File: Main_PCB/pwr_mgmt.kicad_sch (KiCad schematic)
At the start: 22 parts, among them SW201 SW_SPST, U201 TPS2116DRL, U202 TPS62143, U203 AP2112K-3.3

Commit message: First draft of schematic complete. Still need to verify it is correct before proceeding to pcb.
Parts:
- removed BT201, BT202: Battery_Cell, symbol Device:Battery_Cell
- removed C202, C204: 10uF, symbol Device:C
- removed C207: 100nF, symbol Device:C
- removed D201: LED, symbol Device:LED
- removed F201: Fuse, symbol Device:Fuse
- removed R201: 100K, symbol Device:R
- removed R204: 220R, symbol Device:R
- removed SW201: SW_SPST, symbol Switch:SW_SPST
- removed U203: AP2112K-3.3, Package_TO_SOT_SMD:SOT-23-5, symbol Regulator_Linear:AP2112K-3.3
- added C205: 10uF, symbol Device:C_Polarized
- added C206: 22uF, symbol Device:C_Polarized
- added U203: AMS1117-3.3, Package_TO_SOT_SMD:SOT-223-3_TabPin2, symbol Regulator_Linear:AMS1117-3.3
- renumbered C206 to C202, C205 to C204, R203 to R201, R205 to R203, R206 to R204, U202 to U201, U201 to U202
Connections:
- net +3.3V: now also C206.1, U203.2 (VO)
- net +5V: now also C205.1, U203.3 (VI)
- net GND: now also C205.2, C206.2, U203.1 (GND)
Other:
- note added: "5V to 3.3V (AMS1117)"
- note removed: "5V to 3.3V (AP2112K-3.3)"
- note removed: "BATTERIES + FUSE"
- note removed: "Note: use X7R or X5R dielectric capacitor"

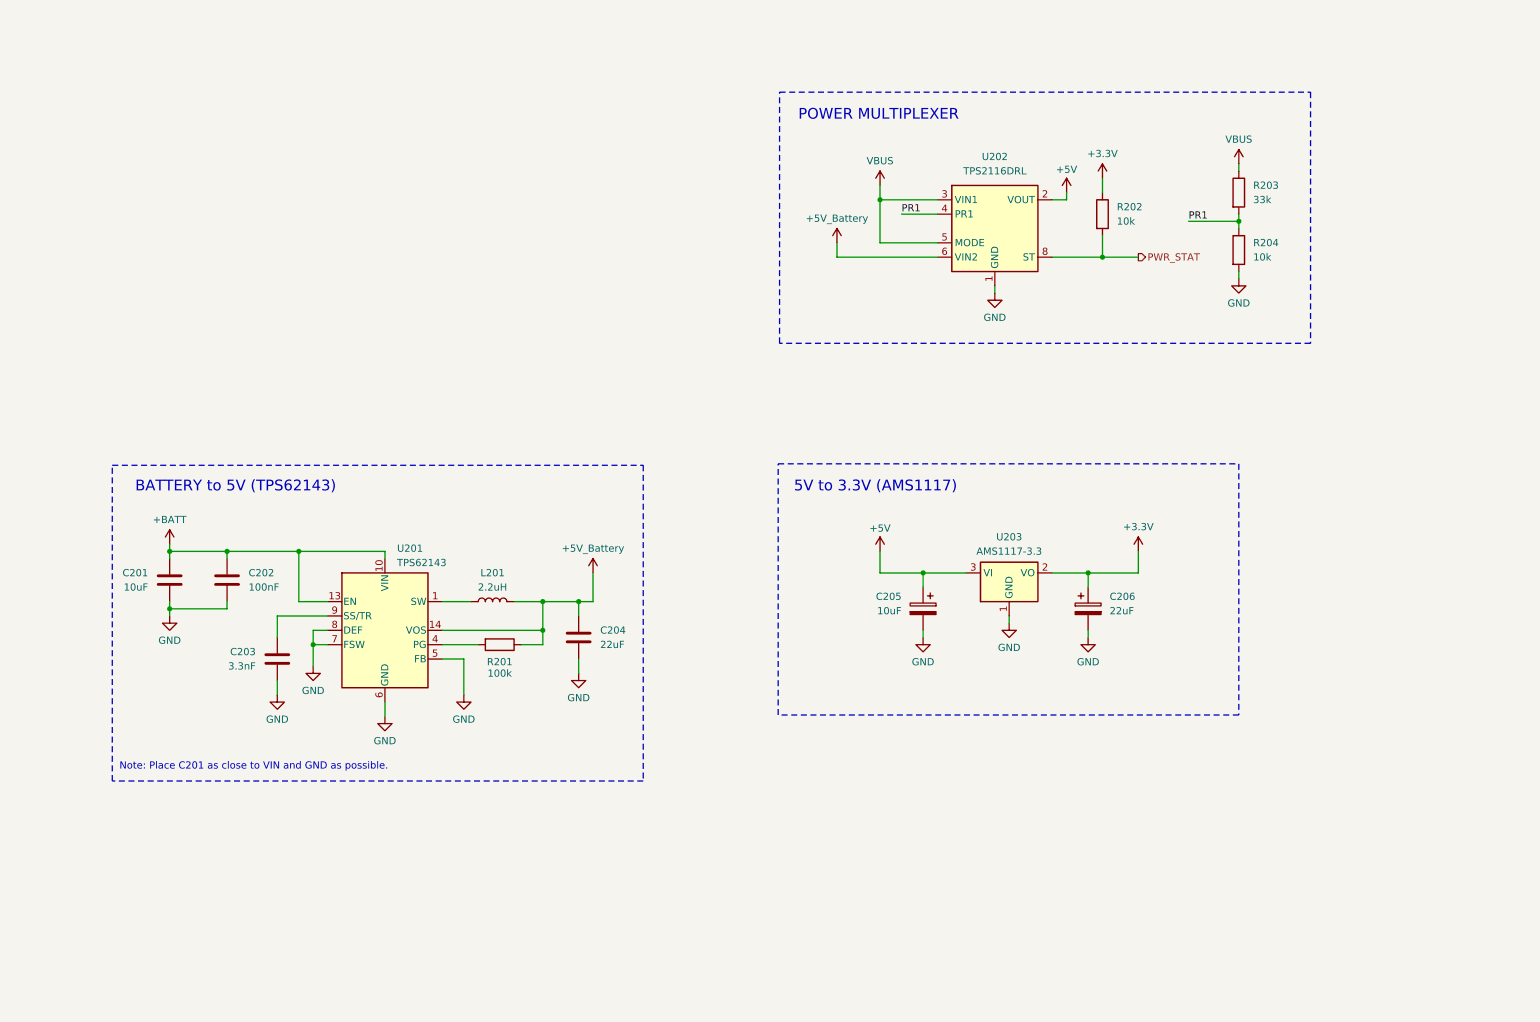
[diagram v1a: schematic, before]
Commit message: Added decoupling capacitors, pulldown resistors, test points, and more. Still need to finish verifying schematic before PCB layout.
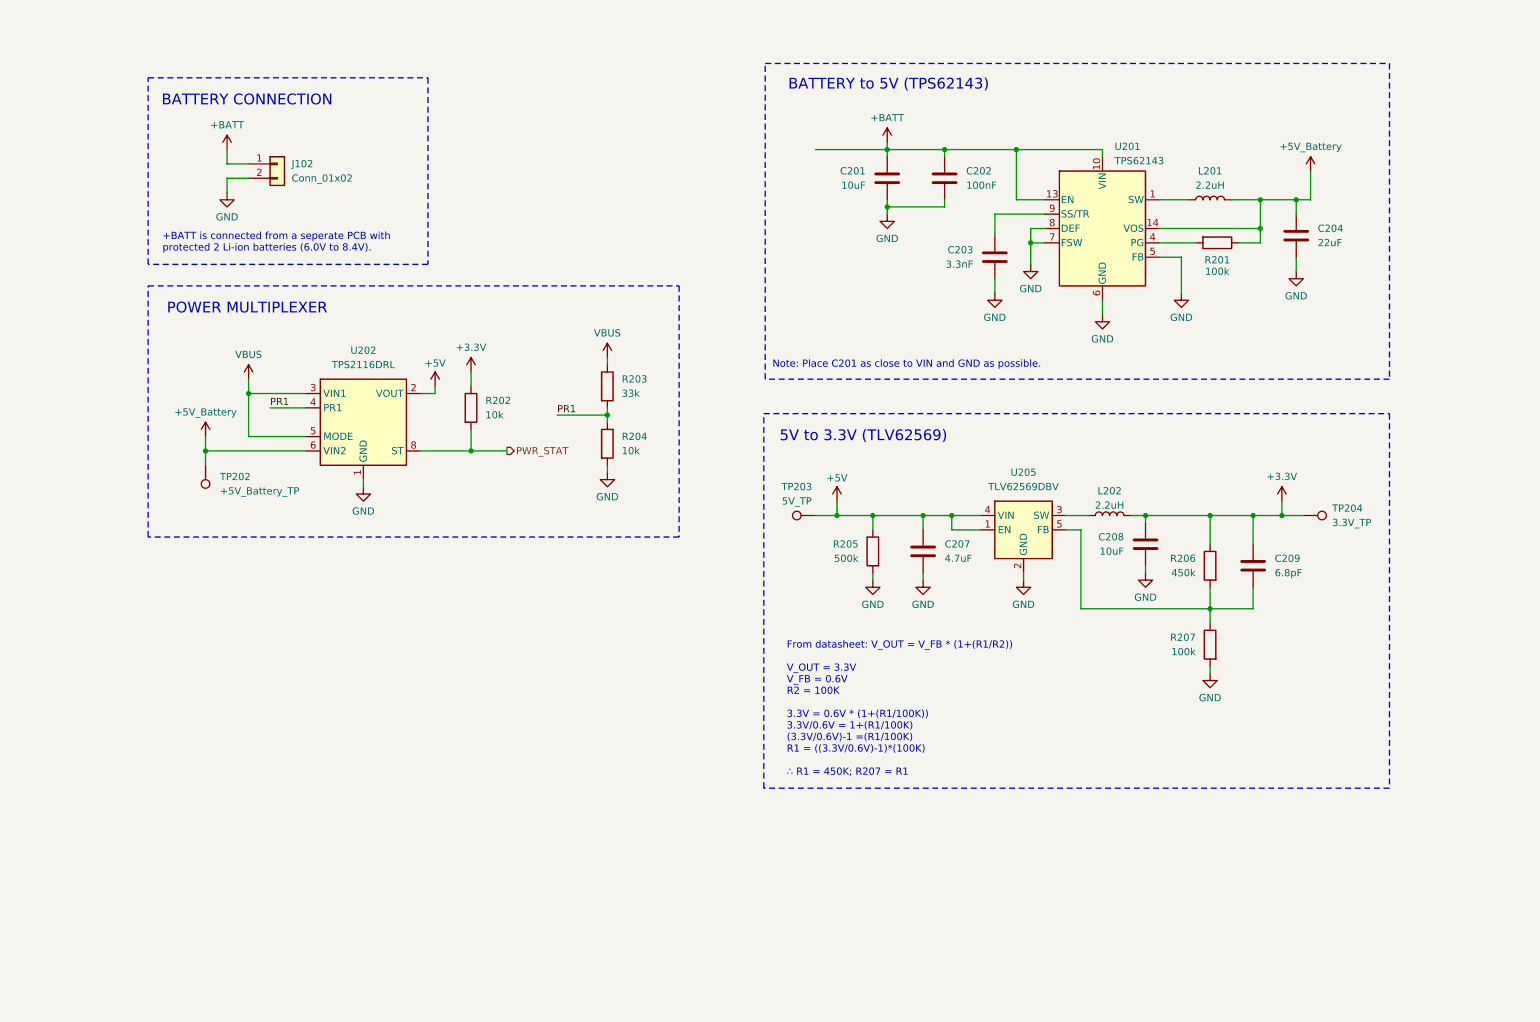
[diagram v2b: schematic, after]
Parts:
- removed C205: 10uF, symbol Device:C_Polarized
- removed C206: 22uF, symbol Device:C_Polarized
- removed U203: AMS1117-3.3, Package_TO_SOT_SMD:SOT-223-3_TabPin2, symbol Regulator_Linear:AMS1117-3.3
- added C207: 4.7uF, symbol Device:C
- added C208: 10uF, symbol Device:C
- added C209: 6.8pF, symbol Device:C
- added J102: Conn_01x02, symbol Connector_Generic:Conn_01x02
- added L202: 2.2uH, symbol Device:L
- added R205: 500k, symbol Device:R
- added R206: 450k, symbol Device:R
- added R207: 100k, symbol Device:R
- added TP202: +5V_Battery_TP, symbol Connector:TestPoint
- added TP203: 5V_TP, symbol Connector:TestPoint
- added TP204: 3.3V_TP, symbol Connector:TestPoint
- added U205: TLV62569DBV, Package_TO_SOT_SMD:SOT-23-5, symbol Regulator_Switching:TLV62569DBV
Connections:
- net +3.3V: now also C208.1, C209.1, L202.2, R206.1, TP204.1
- net +5V: now also C207.1, R205.1, TP203.1, U205.1 (EN), U205.4 (VIN)
- net +5V_Battery: now also TP202.1
- net +BATT: now also J102.1 (Pin_1)
- net GND: now also C207.2, C208.2, J102.2 (Pin_2), R205.2, R207.2, U205.2 (GND)
- new net: C209.2, R206.2, R207.1, U205.5 (FB)
- new net: L202.1, U205.3 (SW)
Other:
- note added: "+BATT is connected from a seperate PCB with protected 2 Li-ion batteries (6.0V to 8.4V)."
- note added: "5V to 3.3V (TLV62569)"
- note added: "BATTERY CONNECTION"
- note added: "From datasheet: V_OUT = V_FB * (1+(R1/R2)) V_OUT = 3.3V V_FB = 0.6V R2 = 100K 3.3V = 0.6V * (1+(R1/100K)) 3.3V/0.6V = 1+(R1/100K) (3.3V/0.6V)-1 =(R1/100K) R1 = ((3.3V/0.6V)-1)*(100K) ∴ R1 = 450K; R207 = R1"
- note removed: "5V to 3.3V (AMS1117)"
- moved on the sheet: C201, C202, C203, C204, L201, R201, R202, R203, R204, U201, U202

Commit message: Adding most recent version of schematic. I have now decided to use NiMH batteries instead of Li-ion because they are safer and I don't want to start a fire.
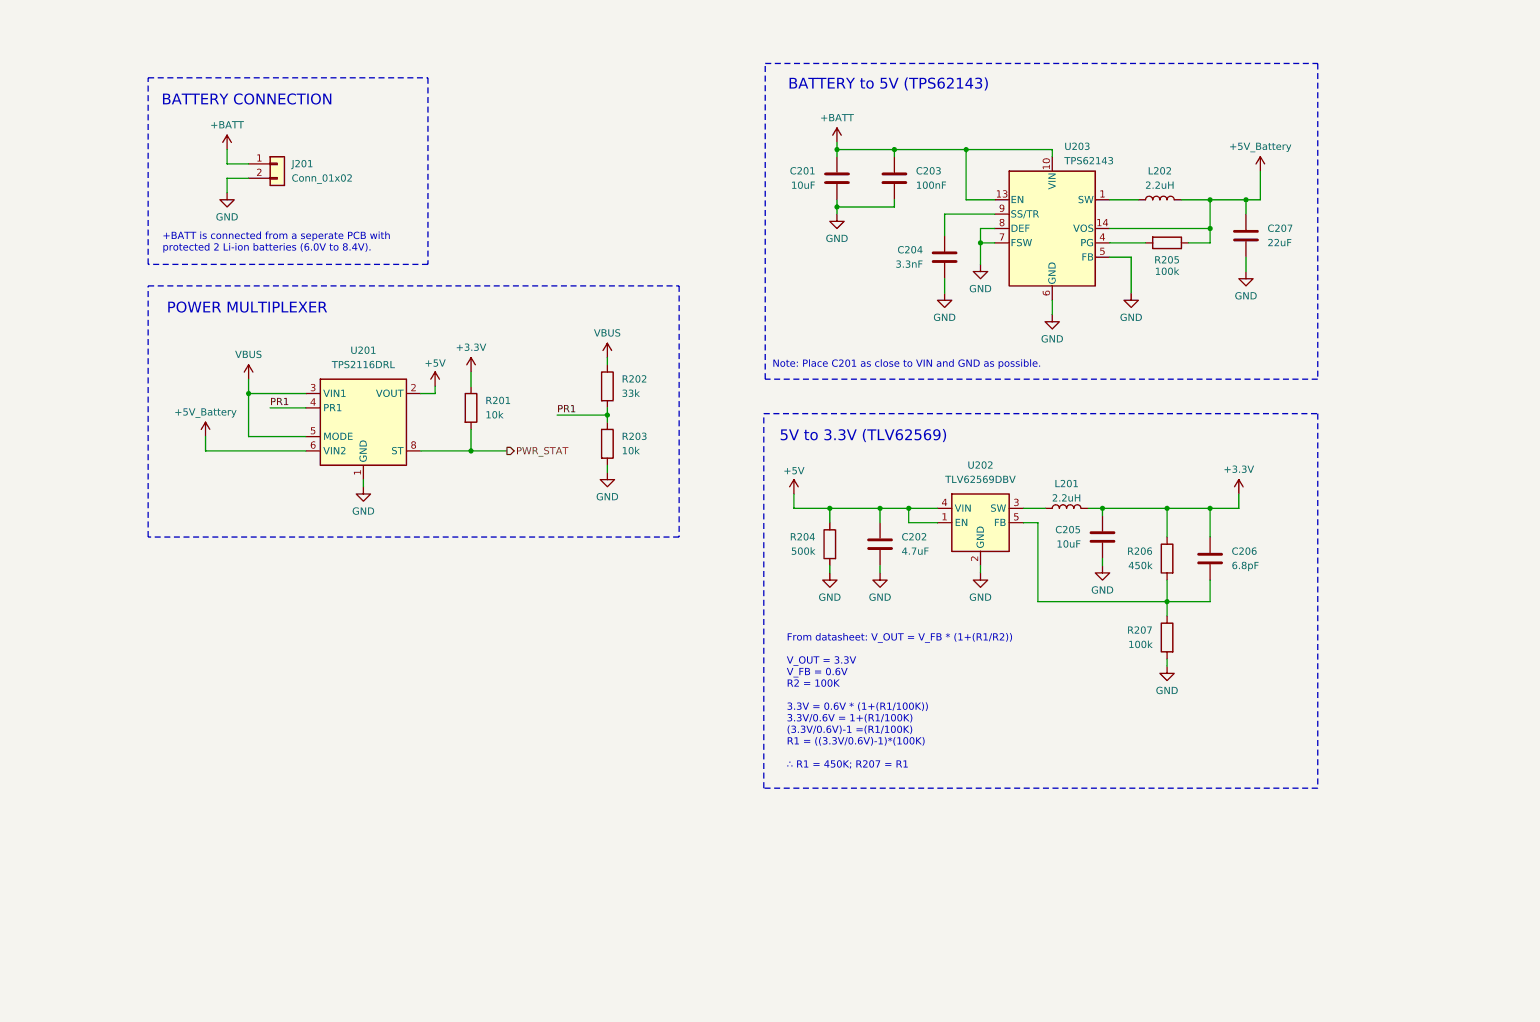
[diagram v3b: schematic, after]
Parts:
- removed TP202: +5V_Battery_TP, symbol Connector:TestPoint
- removed TP203: 5V_TP, symbol Connector:TestPoint
- removed TP204: 3.3V_TP, symbol Connector:TestPoint
- renumbered C207 to C202, C202 to C203, C203 to C204, C208 to C205, C209 to C206, C204 to C207, J102 to J201, L202 to L201, L201 to L202, R202 to R201, R203 to R202, R204 to R203, R205 to R204, R201 to R205, U202 to U201, U205 to U202, U201 to U203
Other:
- moved on the sheet: C201, C202, C203, C204, C205, C206, C207, L201, L202, R204, R205, R206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

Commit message: Adding changes. Changes made to cleanup schematic before pcb layout.
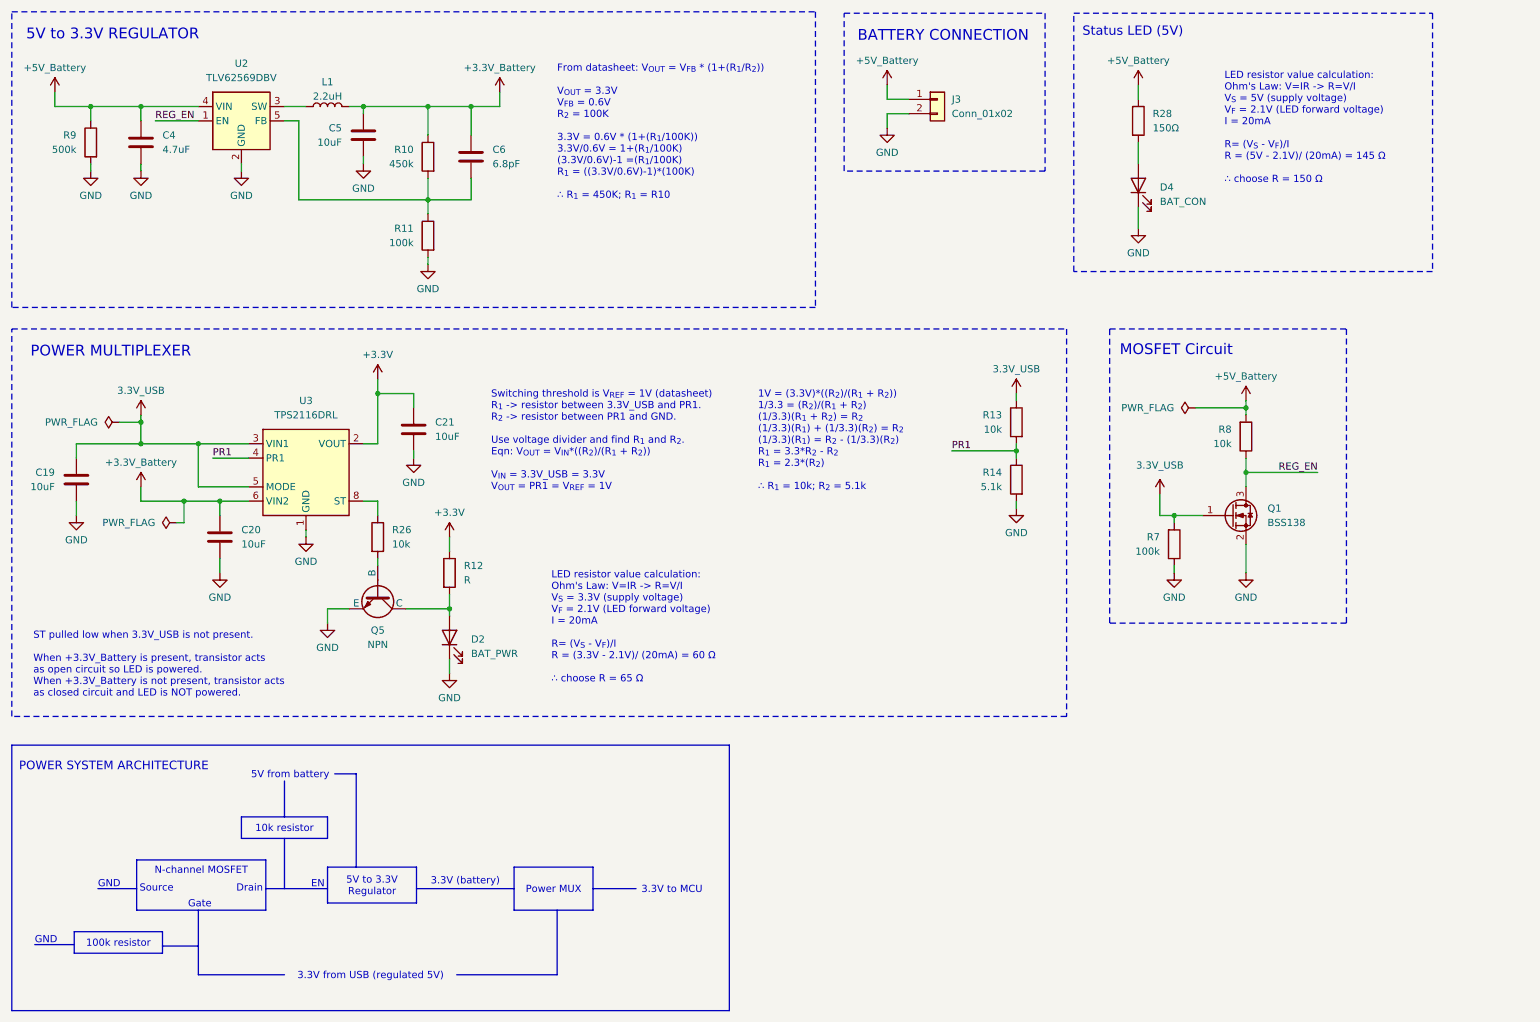
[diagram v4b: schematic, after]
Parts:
- removed C201: 10uF, symbol Device:C
- removed C203: 100nF, symbol Device:C
- removed C204: 3.3nF, symbol Device:C
- removed C207: 22uF, symbol Device:C
- removed L202: 2.2uH, symbol Device:L
- removed R205: 100k, symbol Device:R
- removed U203: TPS62143, Package_DFN_QFN:VQFN-16-1EP_3x3mm_P0.5mm_EP1.68x1.68mm_ThermalVias, symbol Regulator_Switching:TPS62143
- added C19, C20, C21: 10uF, symbol Device:C
- added D2: BAT_PWR, symbol Device:LED
- added D4: BAT_CON, symbol Device:LED
- added Q1: BSS138, Package_TO_SOT_SMD:SOT-23, symbol Transistor_FET:BSS138
- added Q5: NPN, symbol Simulation_SPICE:NPN
- added R26, R8: 10k, symbol Device:R
- added R28: 150Ω, symbol Device:R
- added R7: 100k, symbol Device:R
- R12: renamed from R201; value 10k -> R
- R13: renamed from R202; value 33k -> 10k
- R14: renamed from R203; value 10k -> 5.1k
- renumbered C202 to C4, C205 to C5, C206 to C6, J201 to J3, L201 to L1, R206 to R10, R207 to R11, R204 to R9, U202 to U2, U201 to U3
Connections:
- net +BATT is gone; now on net +5V_Battery: J3.1 (Pin_1)
- net +3.3V: now also U3.2 (VOUT), U3.7 (VOUT), C21.1; no longer C5.1, C6.1, L1.2, R10.1
- net +5V_Battery: now also C4.1, R9.1, U2.4 (VIN), R28.1, R8.2; no longer U3.6 (VIN2)
- net GND: now also C19.2, C20.2, C21.2, D2.1 (K), D4.1 (K), Q1.2 (S), Q5.3 (E), R7.1
- removed net +5V: C4.1, R9.1, U2.1 (EN), U2.4 (VIN), U3.2 (VOUT), U3.7 (VOUT)
- net PWR_STAT: no longer names the net of U3.8 (ST)
- net PWR_STAT: now also R26.1; no longer R12.2
- net VBUS renamed 3.3V_USB
- net 3.3V_USB: now also C19.1, Q1.1 (G), R7.2
- new net: Q5.2 (B), R26.2
- new net: D2.2 (A), Q5.1 (C), R12.2
- new net: D4.2 (A), R28.2
- new net +3.3V_Battery: C20.1, C5.1, C6.1, L1.2, R10.1, U3.6 (VIN2)
- new net REG_EN: Q1.3 (D), R8.1, U2.1 (EN)
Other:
- note added: "1V = (3.3V)*((R_{2})/(R_{1} + R_{2})) 1/3.3 = (R_{2})/(R_{1} + R_{2}) (1/3.3)(R_{1} + R_{2}) = R_{2} (1/3.3)(R_{1}) + (1/3.3)(R_{2}) = R_{2} (1/3.3)(R_{1}) = R_{2} - (1/3.3)(R_{2}) R_{1} = 3.3*R_{2} - R_{2} R_{1} = 2.3*(R_{2}) ∴ R_{1} = 10k; R_{2} = 5.1k"
- note added: "3.3V (battery)"
- note added: "3.3V from USB (regulated 5V)"
- note added: "3.3V to MCU"
- note added: "5V from battery"
- note added: "5V to 3.3V REGULATOR"
- note added: "Drain"
- note added: "EN"
- note added: "From datasheet: V_{OUT} = V_{FB} * (1+(R_{1}/R_{2})) V_{OUT} = 3.3V V_{FB} = 0.6V R_{2} = 100K 3.3V = 0.6V * (1+(R_{1}/100K)) 3.3V/0.6V = 1+(R_{1}/100K) (3.3V/0.6V)-1 =(R_{1}/100K) R_{1} = ((3.3V/0.6V)-1)*(100K) ∴ R_{1} = 450K; R_{1} = R10"
- note added: "GND"
- note added: "Gate"
- note added: "LED resistor value calculation: Ohm's Law: V=IR -> R=V/I V_{S} = 3.3V (supply voltage) V_{F} = 2.1V (LED forward voltage) I = 20mA R= (V_{S} - V_{F})/I R = (3.3V - 2.1V)/ (20mA) = 60 Ω ∴ choose R = 65 Ω"
- note added: "LED resistor value calculation: Ohm's Law: V=IR -> R=V/I V_{S} = 5V (supply voltage) V_{F} = 2.1V (LED forward voltage) I = 20mA R= (V_{S} - V_{F})/I R = (5V - 2.1V)/ (20mA) = 145 Ω ∴ choose R = 150 Ω"
- note added: "MOSFET Circuit"
- note added: "POWER SYSTEM ARCHITECTURE"
- note added: "ST pulled low when 3.3V_USB is not present. When +3.3V_Battery is present, transistor acts as open circuit so LED is powered. When +3.3V_Battery is not present, transistor acts as closed circuit and LED is NOT powered."
- note added: "Source"
- note added: "Status LED (5V)"
- note added: "Switching threshold is V_{REF} = 1V (datasheet) R_{1} -> resistor between 3.3V_USB and PR1. R_{2} -> resistor between PR1 and GND. Use voltage divider and find R_{1} and R_{2}. Eqn: V_{OUT} = V_{IN}*((R_{2})/(R_{1} + R_{2})) V_{IN} = 3.3V_USB = 3.3V V_{OUT} = PR1 = V_{REF} = 1V"
- note removed: "+BATT is connected from a seperate PCB with protected 2 Li-ion batteries (6.0V to 8.4V)."
- note removed: "5V to 3.3V (TLV62569)"
- note removed: "BATTERY to 5V (TPS62143)"
- note removed: "From datasheet: V_OUT = V_FB * (1+(R1/R2)) V_OUT = 3.3V V_FB = 0.6V R2 = 100K 3.3V = 0.6V * (1+(R1/100K)) 3.3V/0.6V = 1+(R1/100K) (3.3V/0.6V)-1 =(R1/100K) R1 = ((3.3V/0.6V)-1)*(100K) ∴ R1 = 450K; R207 = R1"
- note removed: "Note: Place C201 as close to VIN and GND as possible."
- moved on the sheet: C4, C5, C6, J3, L1, R10, R11, R12, R13, R14, R9, U2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

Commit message: Removed MOSFET circuit from power management subsystem.
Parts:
- removed Q1: BSS138, Package_TO_SOT_SMD:SOT-23, symbol Transistor_FET:BSS138
- removed R7: 100k, symbol Device:R
- removed R8: 10k, symbol Device:R
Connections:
- net REG_EN is gone; now on net +5V_Battery: U2.1 (EN)
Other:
- note removed: "3.3V (battery)"
- note removed: "3.3V from USB (regulated 5V)"
- note removed: "3.3V to MCU"
- note removed: "5V from battery"
- note removed: "Drain"
- note removed: "EN"
- note removed: "GND"
- note removed: "Gate"
- note removed: "MOSFET Circuit"
- note removed: "POWER SYSTEM ARCHITECTURE"
- note removed: "Source"
- moved on the sheet: D4, R28
